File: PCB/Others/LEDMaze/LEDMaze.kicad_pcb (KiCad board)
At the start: 2 copper layers, 79 x 59 mm, 78 parts, among them J1 In, J2 Out

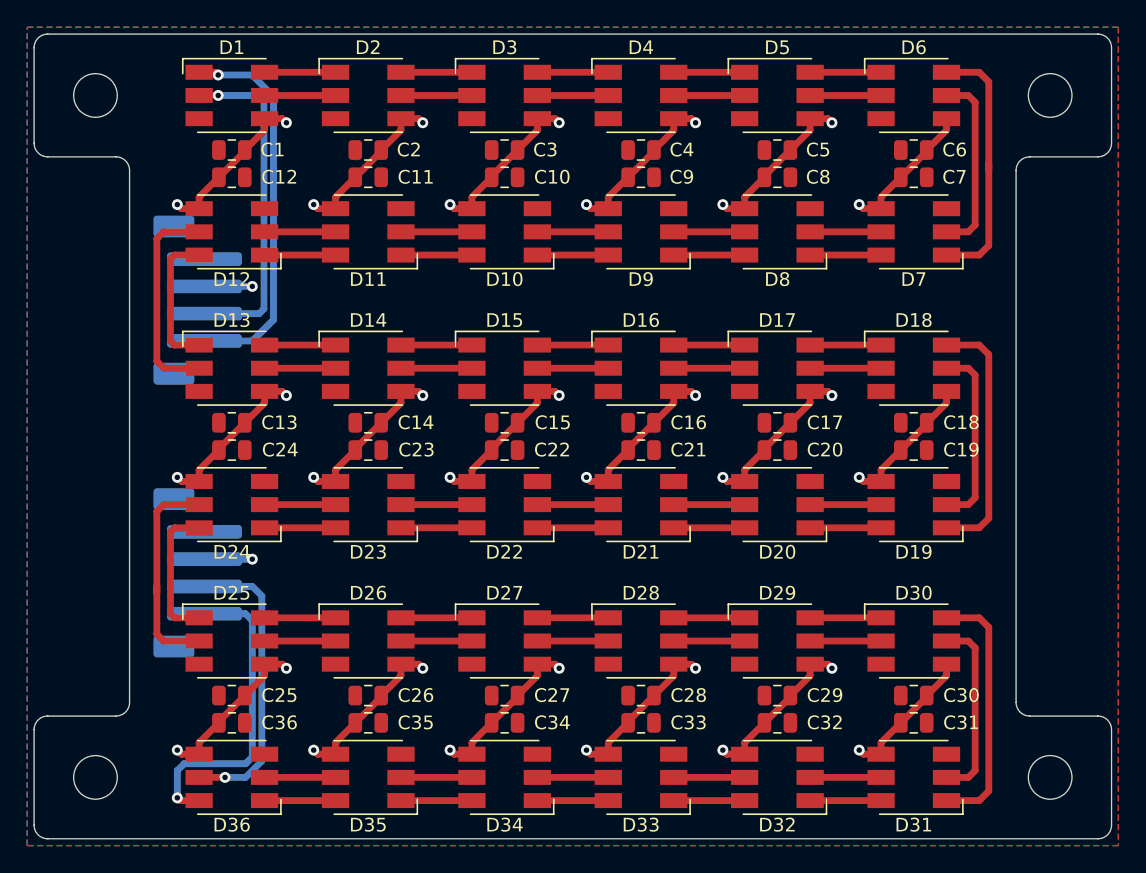
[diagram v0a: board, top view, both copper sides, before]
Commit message: Convert all KiCad to 6.0, clean up libraries, remove files that shouldn't be committed.
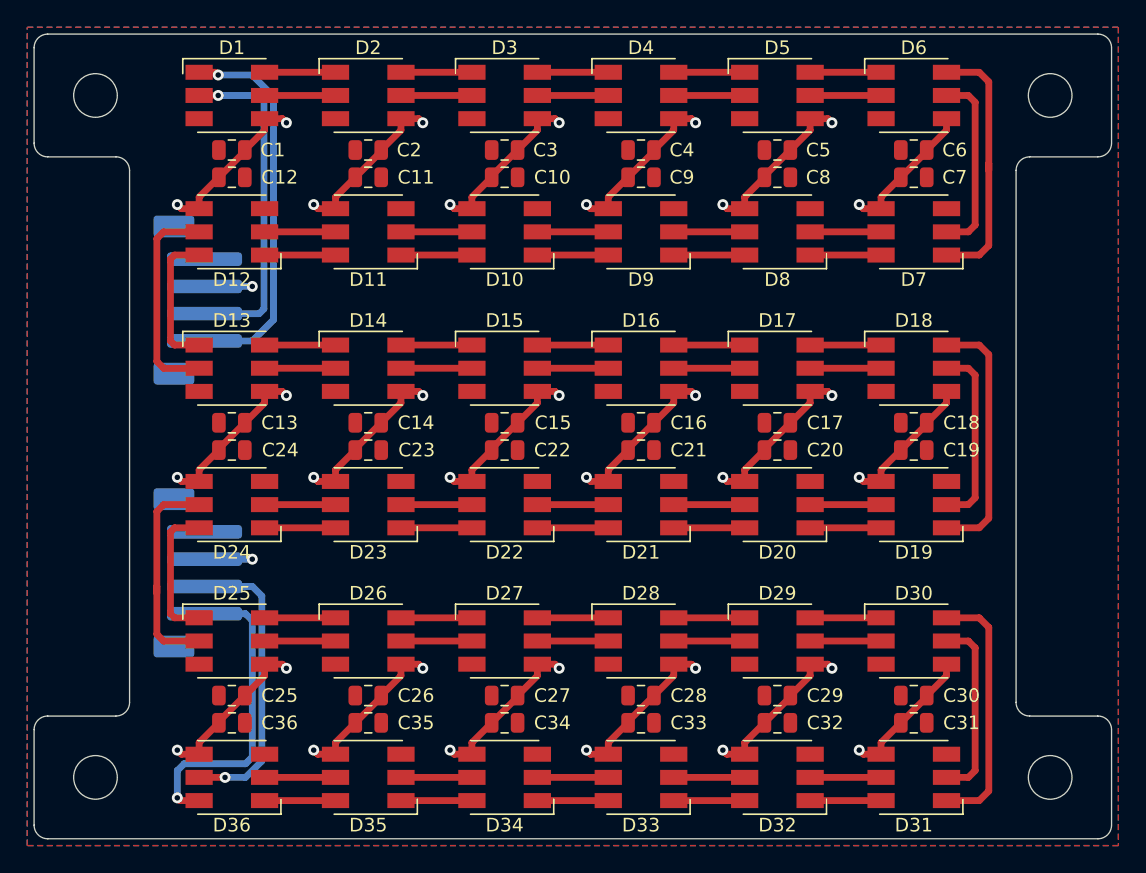
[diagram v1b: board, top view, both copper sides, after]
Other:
- net class Default removed
